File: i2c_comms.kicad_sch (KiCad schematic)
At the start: 12 parts

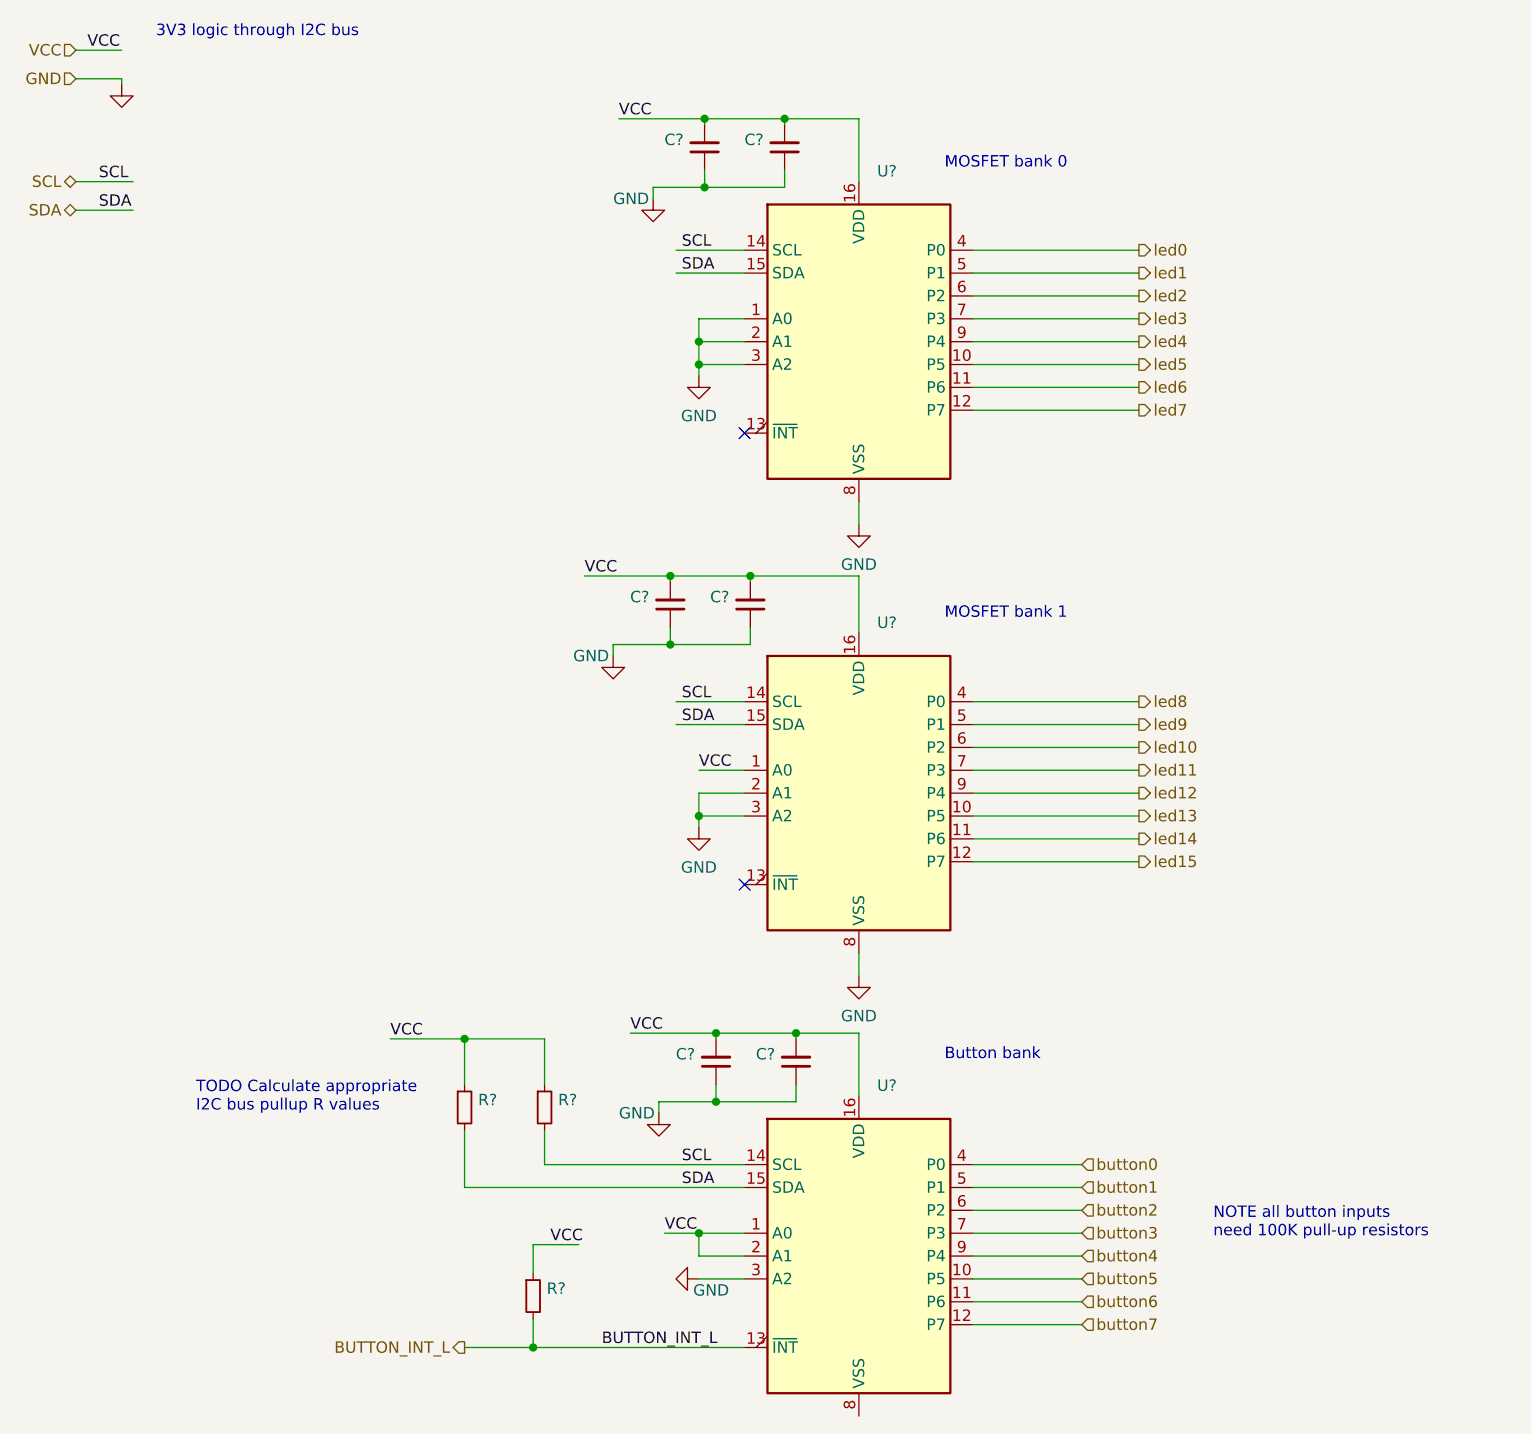
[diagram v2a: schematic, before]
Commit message: Sketch out ISL8117-driven 12V regulator.
Another candidate entry for on-board 12V regulation is to
build our own based on the reference schematic from the ISL8117
DC buck regulator controller datasheet.

Implemented (most of) this reference schematic here.
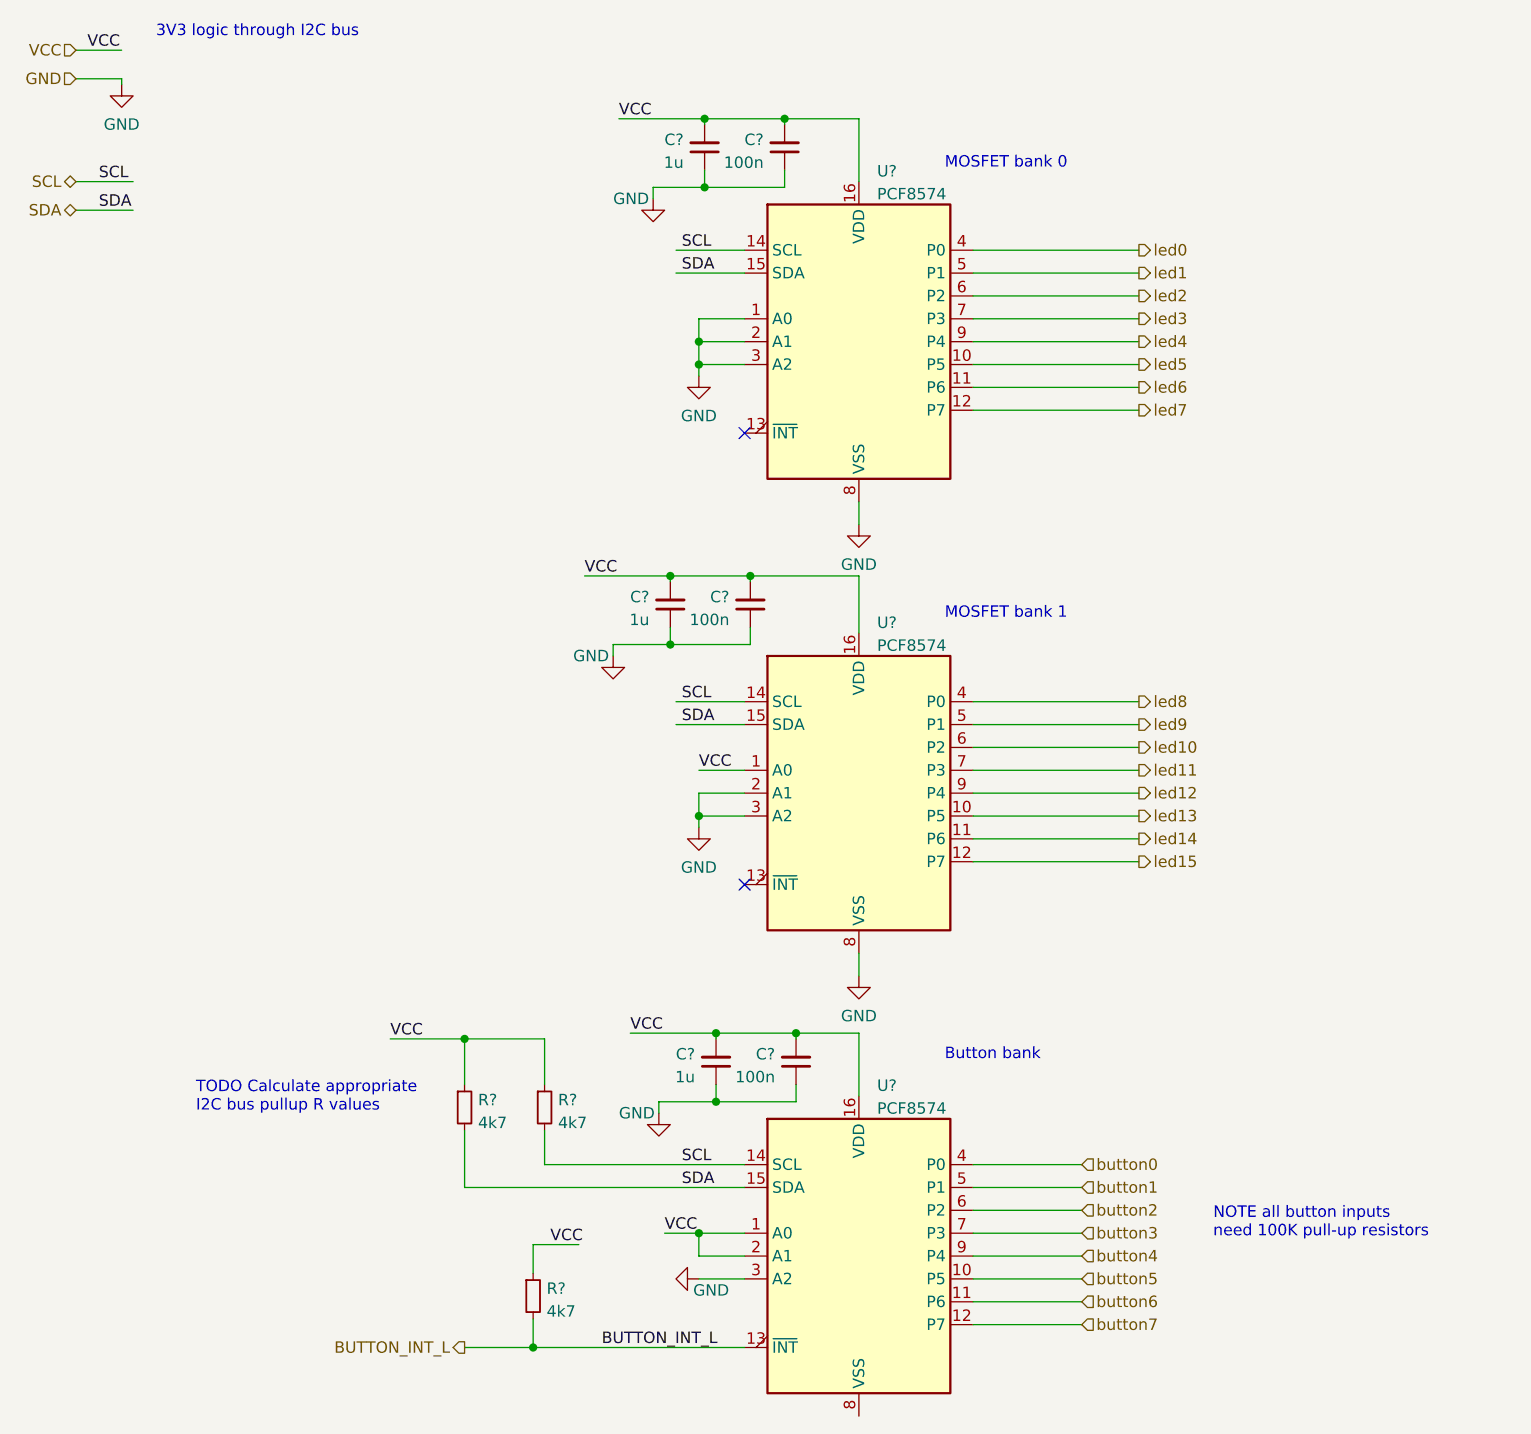
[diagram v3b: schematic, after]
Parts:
- C? (x3): value (none) -> 100n
- C? (x3): value (none) -> 1u
- R? (x3): value (none) -> 4k7
- U? (x3): value (none) -> PCF8574
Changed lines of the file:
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@@
       (effects (font (size 1.27 1.27)) (justify left))
     )
-    (property "Value" "" (id 1) (at 77.0636 137.5922 0)
+    (property "Value" "4k7" (id 1) (at 77.0636 137.5922 0)
       (effects (font (size 1.27 1.27)) (justify left))
     )
@@
       (effects (font (size 1.27 1.27)) (justify right))
     )
-    (property "Value" "" (id 1) (at 101.1809 132.5058 0)
+    (property "Value" "100n" (id 1) (at 101.1809 132.5058 0)
       (effects (font (size 1.27 1.27)) (justify right))
     )
@@
       (effects (font (size 1.27 1.27)) (justify left))
     )
-    (property "Value" "" (id 1) (at 75.7936 158.5472 0)
+    (property "Value" "4k7" (id 1) (at 75.7936 158.5472 0)
       (effects (font (size 1.27 1.27)) (justify left))
     )
@@
       (effects (font (size 1.27 1.27)) (justify right))
     )
-    (property "Value" "" (id 1) (at 87.2109 81.7058 0)
+    (property "Value" "1u" (id 1) (at 87.2109 81.7058 0)
       (effects (font (size 1.27 1.27)) (justify right))
     )
@@
       (effects (font (size 1.27 1.27)) (justify right))
     )
-    (property "Value" "" (id 1) (at 91.0209 30.9058 0)
+    (property "Value" "1u" (id 1) (at 91.0209 30.9058 0)
       (effects (font (size 1.27 1.27)) (justify right))
     )
@@
       (effects (font (size 1.27 1.27)) (justify right))
     )
-    (property "Value" "" (id 1) (at 96.1009 81.7058 0)
+    (property "Value" "100n" (id 1) (at 96.1009 81.7058 0)
       (effects (font (size 1.27 1.27)) (justify right))
     )
@@
       (effects (font (size 1.27 1.27)) (justify right))
     )
-    (property "Value" "" (id 1) (at 99.9109 30.9058 0)
+    (property "Value" "100n" (id 1) (at 99.9109 30.9058 0)
       (effects (font (size 1.27 1.27)) (justify right))
     )
@@
       (effects (font (size 1.27 1.27)) (justify left))
     )
-    (property "Value" "" (id 1) (at 112.5094 84.5621 0)
+    (property "Value" "PCF8574" (id 1) (at 112.5094 84.5621 0)
       (effects (font (size 1.27 1.27)) (justify left))
     )
@@
       (effects (font (size 1.27 1.27)) hide)
     )
-    (property "Value" "" (id 1) (at 28.575 26.6684 0))
+    (property "Value" "GND" (id 1) (at 28.575 26.6684 0))
     (property "Footprint" "" (id 2) (at 28.575 22.225 0)
       (effects (font (size 1.27 1.27)) hide)
@@
       (effects (font (size 1.27 1.27)) (justify left))
     )
-    (property "Value" "" (id 1) (at 68.1736 137.5922 0)
+    (property "Value" "4k7" (id 1) (at 68.1736 137.5922 0)
       (effects (font (size 1.27 1.27)) (justify left))
     )
@@
       (effects (font (size 1.27 1.27)) (justify left))
     )
-    (property "Value" "" (id 1) (at 112.5094 34.3971 0)
+    (property "Value" "PCF8574" (id 1) (at 112.5094 34.3971 0)
       (effects (font (size 1.27 1.27)) (justify left))
     )
@@
       (effects (font (size 1.27 1.27)) (justify right))
     )
-    (property "Value" "" (id 1) (at 92.2909 132.5058 0)
+    (property "Value" "1u" (id 1) (at 92.2909 132.5058 0)
       (effects (font (size 1.27 1.27)) (justify right))
     )
@@
       (effects (font (size 1.27 1.27)) (justify left))
     )
-    (property "Value" "" (id 1) (at 112.5094 135.9971 0)
-      (effects (font (size 1.27 1.27)) (justify left))
-    )
+    (property "Value" "PCF8574" (id 1) (at 112.5094 135.9971 0)
+      (effects (font (size 1.27 1.27)) (justify left))
+    )
